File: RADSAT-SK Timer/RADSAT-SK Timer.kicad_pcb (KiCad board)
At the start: 2 copper layers, 90.2 x 95.9 mm, 124 parts, among them J101 Conn_02x26_Odd_Even, J103 Conn_02x26_Odd_Even, J201 Conn_01x07, J202 Conn_01x05, J203 Conn_01x03, J204 Conn_01x02, J205 Conn_01x02, J206 Conn_01x02, Q101 IRLML2060, Q102 IRLML2060, Q103 IRLML2060, Q104 IRLML2060, Q105 IRLML2060, Q106 IRLML2060, Q107 IRLML2060, Q108 IRLML2060, Q109 IRLML2060, Q201 IRLML2060, Q202 IRLML2060, Q204 IRLML2060, Q205 IRLML2060, Q206 IRLML2060, Q207 IRLML2060, SW201 SW_Push, SW202 SW_Push, SW203 SW_Push, SW204 SW_Push, SW205 SW_Push, SW206 SW_Push, U101 LM397MF, U102 LM397MF, U103 LM397MF, U104 CD4052B, U202 LTC3440EMSPBF, U230 CPC1117N, U240 CPC1117N, U250 CPC1117N, U260 CPC1117N

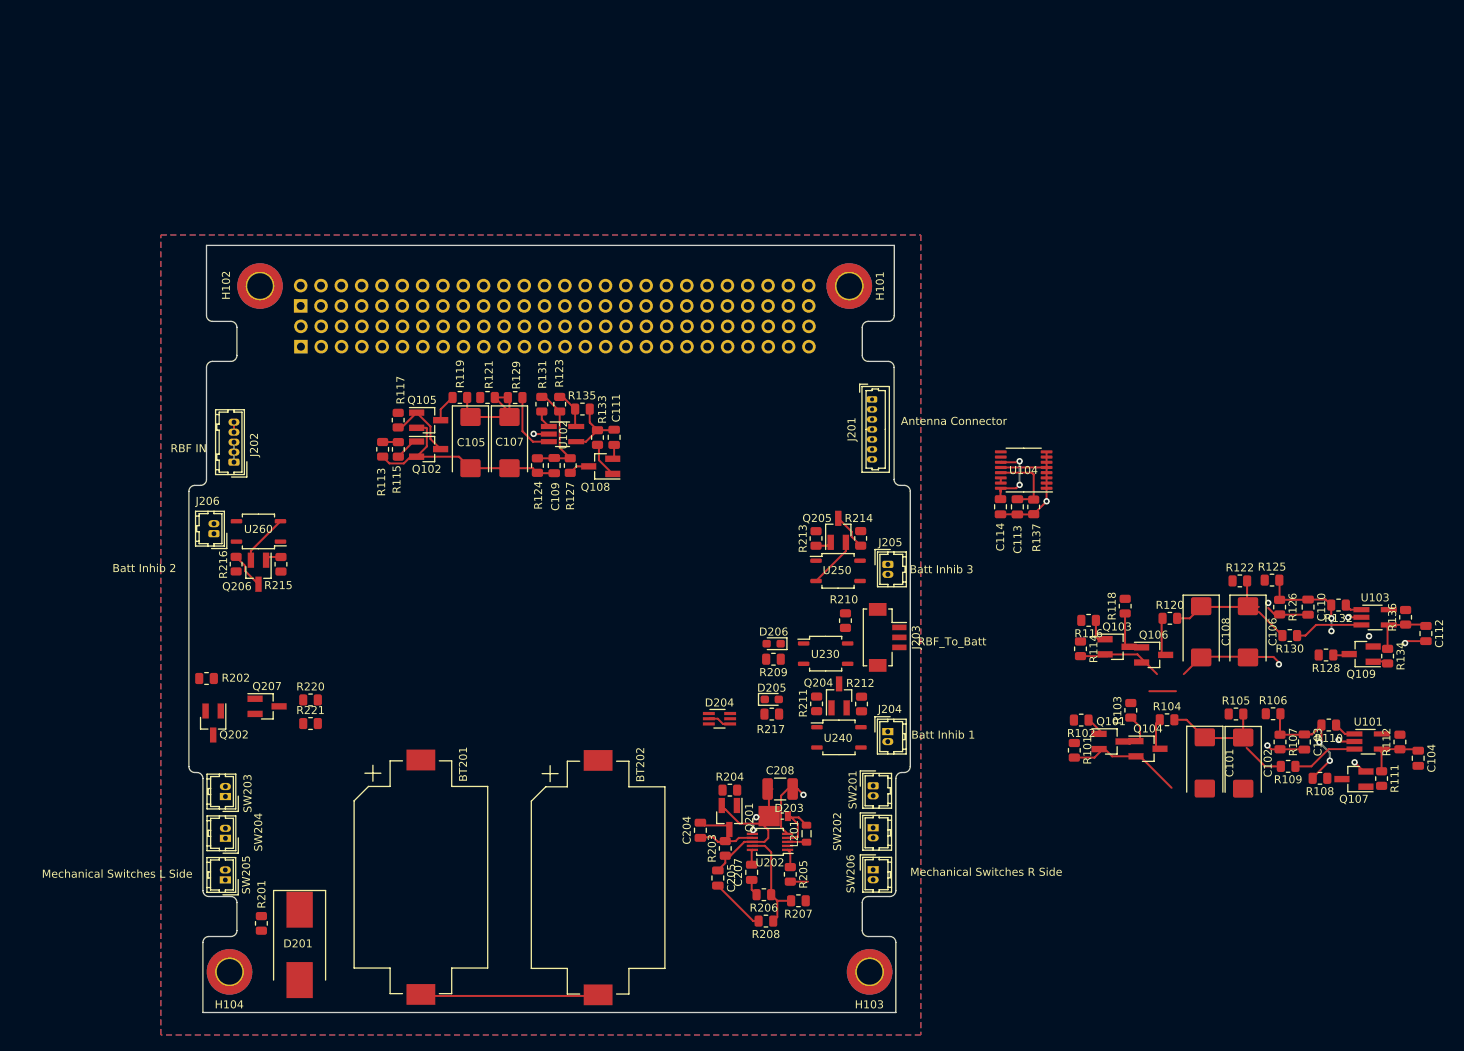
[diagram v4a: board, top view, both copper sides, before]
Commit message: Timer circuit layouts, next up is buck booster
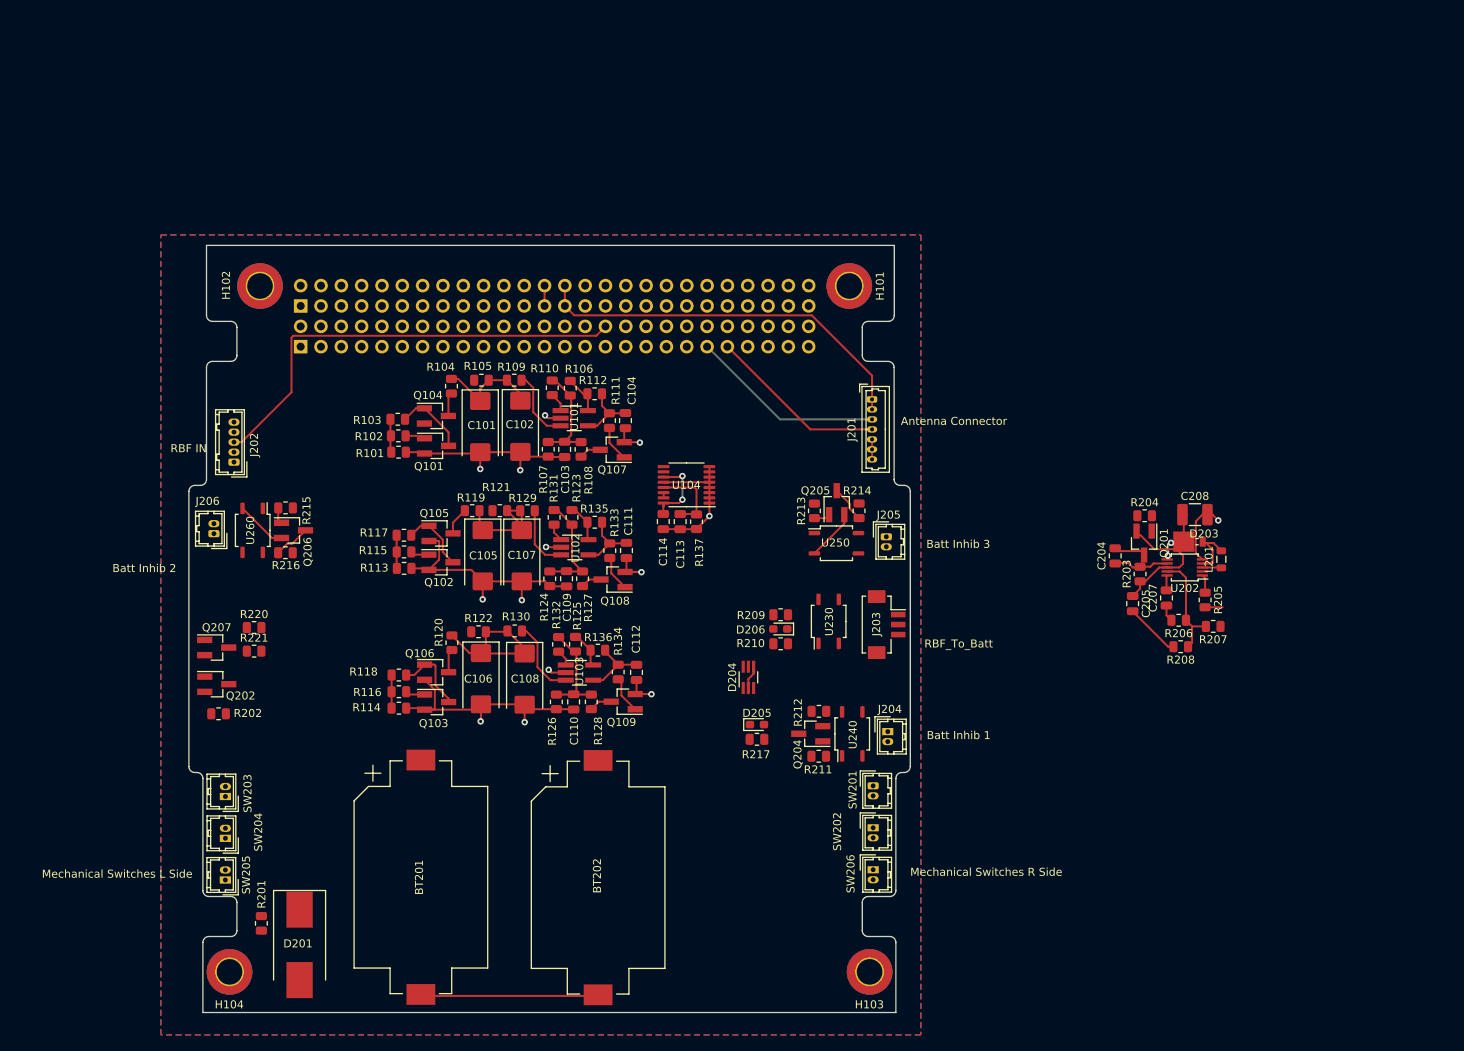
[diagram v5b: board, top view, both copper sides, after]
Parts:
- moved R112 109.7 mm to (85.5, 68.5), turned to 180 degrees
- moved R109 108.1 mm to (75.5, 66.8)
- moved C104 107.7 mm to (89.4, 71.9)
- moved U101 107.2 mm to (83.0, 71.6)
- moved R111 106.4 mm to (87.4, 71.9)
- moved R110 105.8 mm to (80.2, 67.8), turned to 90 degrees
- moved R105 103.1 mm to (71.4, 66.8)
- moved Q107 101.4 mm to (87.8, 75.5)
- moved R108 101.1 mm to (83.8, 75.5), turned to 90 degrees
- moved R136 101.1 mm to (86.0, 100.6), turned to 180 degrees
- moved C101 99.9 mm to (71.2, 72.7)
- moved U103 99.7 mm to (83.7, 103.4)
- moved C102 99.7 mm to (76.3, 72.6)
- moved C103 99.4 mm to (81.8, 75.5)
- moved C112 98.8 mm to (90.8, 103.4)
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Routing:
- net USB_Charge: track 0.00 -> 56.4 mm
- net +3V3: track 0.00 -> 48.8 mm
- net I2C_DATA: track 0.00 -> 24.4 mm
- net I2C_CLK: track 0.00 -> 22.3 mm
- net +BATT: track 23.9 -> 43.9 mm
- net GND: track 132.3 -> 146.4 mm, vias 11 -> 14
- net Net-(C101-Pad1): track 18.1 -> 13.3 mm
- net Net-(Q107-Pad1): track 0.00 -> 4.47 mm
- net Net-(C103-Pad1): track 16.4 -> 13.3 mm, vias 2 -> 0
- net Net-(Q101-Pad3): track 6.05 -> 8.95 mm
- net Net-(Q107-Pad3): track 0.00 -> 2.76 mm
- net Net-(Q103-Pad3): track 6.77 -> 9.48 mm
- net +5V: track 2.93 -> 5.47 mm
- net Net-(D201-Pad1): track 2.50 -> 0.00 mm
- net Net-(Q109-Pad1): track 2.39 -> 4.63 mm
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
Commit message: Layout ios near complete just need to make custom inductor footprint
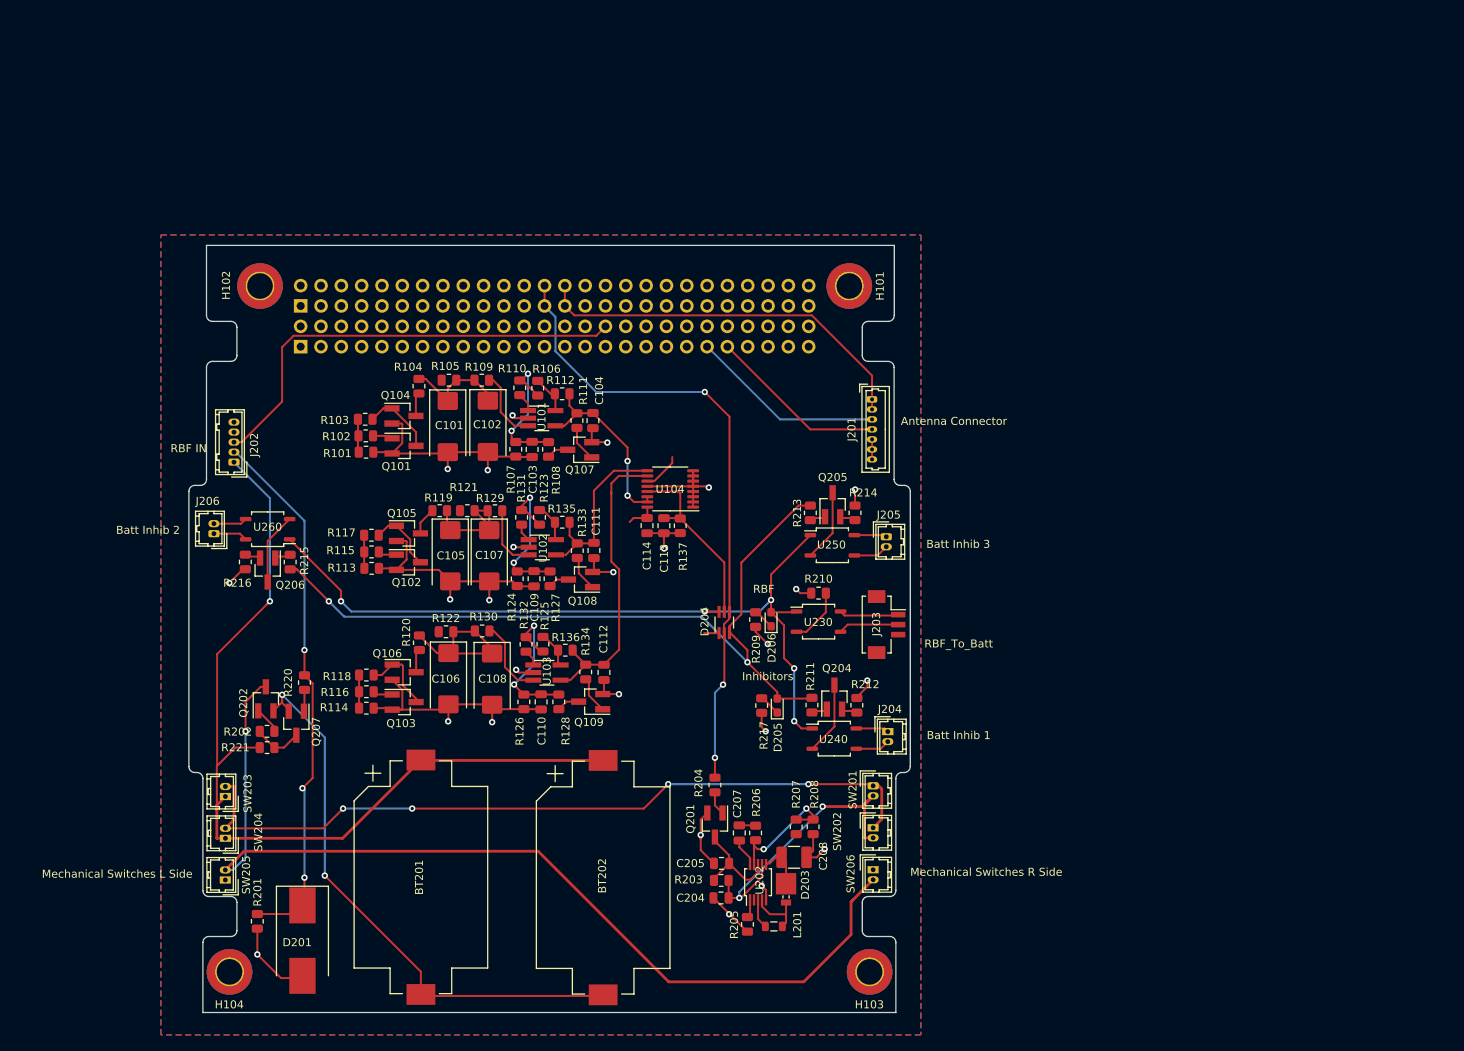
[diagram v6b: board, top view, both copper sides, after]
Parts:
- added G***: LOGO, USSTlogo:USSTLOGO, B.Cu at (79.2, 85.3)
- moved L201 72.3 mm to (108.0, 135.1), turned to 0 degrees
- moved R205 70.1 mm to (104.6, 134.9)
- moved D203 66.6 mm to (109.5, 130.5), turned to 270 degrees
- moved U202 66.3 mm to (106.0, 129.6), turned to 90 degrees
- moved C208 65.9 mm to (110.5, 126.5)
- moved C204 65.2 mm to (101.3, 131.6), turned to 180 degrees
- moved R203 64.9 mm to (101.4, 129.4), turned to 0 degrees
- moved Q201 64.2 mm to (100.6, 122.5)
- moved R204 63.4 mm to (100.6, 117.5), turned to 270 degrees
- moved C207 60.9 mm to (103.6, 123.4), turned to 270 degrees
- moved C205 60.8 mm to (101.4, 127.3), turned to 180 degrees
- moved R206 59.2 mm to (105.7, 123.4), turned to 90 degrees
- moved R207 57.8 mm to (110.7, 122.7), turned to 90 degrees
- moved R208 51.2 mm to (112.9, 122.7), turned to 270 degrees
- moved Q207 13.7 mm to (48.3, 109.7), turned to 270 degrees
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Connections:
- net Net-(D204-Pad3) renamed /RADSAT-SK Timer 2/Inhib_in
- SW203 pad 2: Net-(SW203-Pad2) -> Net-(SW201-Pad1)
- SW204 pad 2: Net-(SW203-Pad2) -> Net-(SW201-Pad1)
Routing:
- net Net-(Q202-Pad3): track 0.00 -> 126.2 mm, vias 0 -> 1
- net Net-(BT201-Pad1): track 0.00 -> 112.7 mm, vias 0 -> 1
- net InhibV+: track 0.00 -> 99.4 mm, vias 0 -> 5
- net /RADSAT-SK Timer 2/Inhib_in: track 0.00 -> 98.1 mm, vias 0 -> 2
- net Net-(SW201-Pad1): track 0.00 -> 96.6 mm, vias 0 -> 4
- net +5V: track 5.47 -> 79.8 mm, vias 0 -> 3
- net Net-(D201-Pad1): track 0.00 -> 66.9 mm, vias 0 -> 3
- net Net-(BT201-Pad2): track 23.0 -> 73.3 mm, vias 0 -> 2
- net GND: track 146.4 -> 179.1 mm, vias 14 -> 25
- net Net-(C204-Pad1): track 6.88 -> 38.5 mm, vias 0 -> 2
- net Timer_C_out: track 8.72 -> 38.3 mm
- net Timer_A_out: track 8.83 -> 23.8 mm, vias 0 -> 2
- net Timer_B_out: track 8.40 -> 22.6 mm
- net Inhib_EN: track 9.41 -> 23.4 mm
- net Net-(Q204-Pad3): track 0.00 -> 9.10 mm
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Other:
- board text added: "Inhibitors"
- board text added: "Project Made Possible By Don Seaman Joseph Remai Don Listwin Mark Teed"
- board text added: "RBF"

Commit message: Modified Inductor Footprint, fixed 3d Model orientation, generated gerbers and drill files. Still unsure about ESD Protection, but can simply remove components from board later.
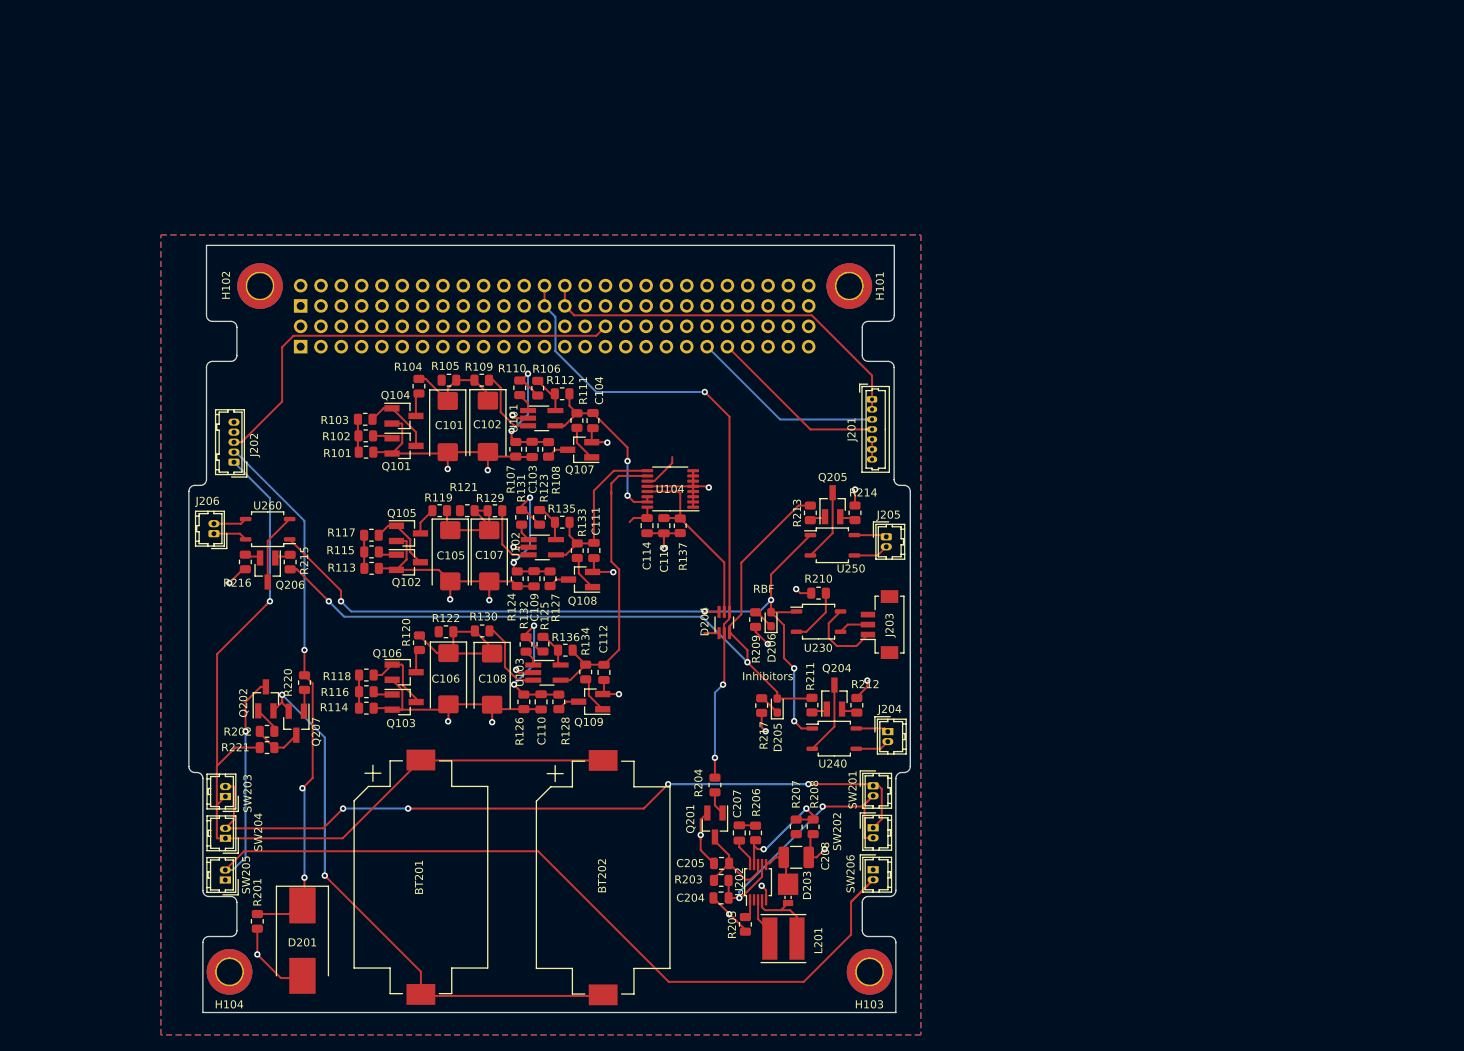
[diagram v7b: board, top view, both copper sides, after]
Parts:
- L201: footprint Inductor_SMD:L_0805_2012Metric -> Sumida_inductor:Sumida_inductor
- moved L201 1.61 mm to (107.4, 136.7)
- moved J203 0.89 mm to (121.2, 97.4), turned to 90 degrees
- moved G*** 0.73 mm to (78.6, 84.9)
- moved C208 0.27 mm to (110.7, 126.5)
- moved D203 0.26 mm to (109.7, 130.6)
- moved R205 0.25 mm to (104.4, 134.9)
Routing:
- net Net-(J203-Pad2): track 7.58 -> 3.79 mm
- net Net-(J203-Pad1): track 7.47 -> 9.83 mm
- net Net-(D203-Pad2): track 7.41 -> 9.76 mm
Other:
- board text added: "B"
- board text added: "November 6th, 2021"
- board text removed: "D"
- board text removed: "For Instructional Use Only."
- board text removed: "January 15, 2021"
- board text removed: "SOLIDWORKS Educational Product."

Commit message: added CSA to the list of donors
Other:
- board text added: "Canadian Space Agency"
